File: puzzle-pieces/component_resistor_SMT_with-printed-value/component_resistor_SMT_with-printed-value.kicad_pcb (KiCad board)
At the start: 2 copper layers, 40 x 40 mm, 11 parts, among them J1 Conn_01x02_Pin, J2 Conn_01x02_Pin

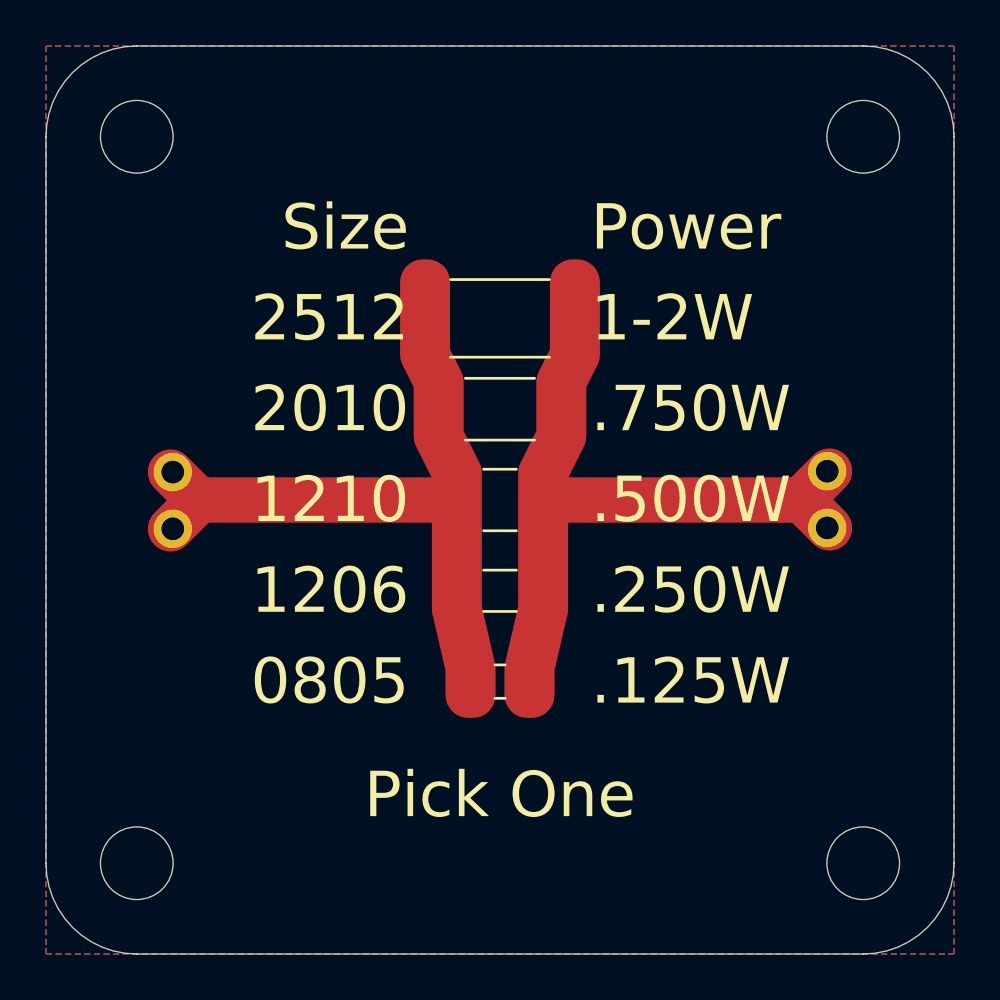
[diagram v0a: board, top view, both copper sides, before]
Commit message: Update resistor footprints and add THT 3W production files
Replaced mounting hole footprints with SMD resistor footprints in the SMT E-6 series panel and updated net assignments. Added new KiCad PCB, project, and production ZIP files for the THT 3W E-6 series resistors. Updated connector reference and position in the SMT panel.
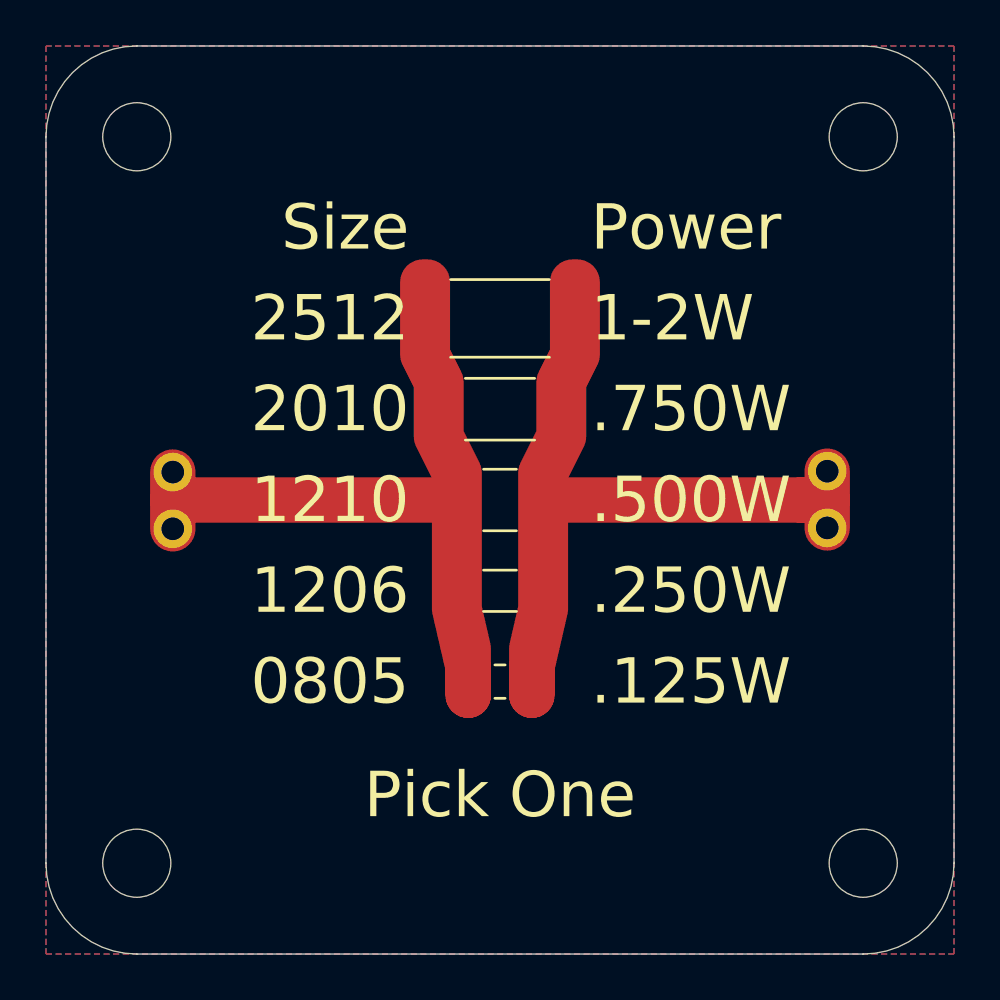
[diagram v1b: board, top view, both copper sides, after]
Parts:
- H1, H2, H3, H4: footprint MountingHole:MountingHole_3.2mm_M3 -> EASYEDA2KICAD:MountingHole_3.0mm_M3_tight
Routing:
- net Net-(J2-Pin_1): track 14.8 -> 16.0 mm
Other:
- board text added: "10 Ω"
- board text removed: "470 Ω"

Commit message: Update resistor value and PCB artwork to 10kΩ
Changed the silkscreen text from '10Ω' to '10kΩ' and updated associated PCB artwork and mask color definitions. Modified polygon and text elements in the KiCad PCB file and replaced the TOP and BOTTOM PNG images to reflect the new value and design.
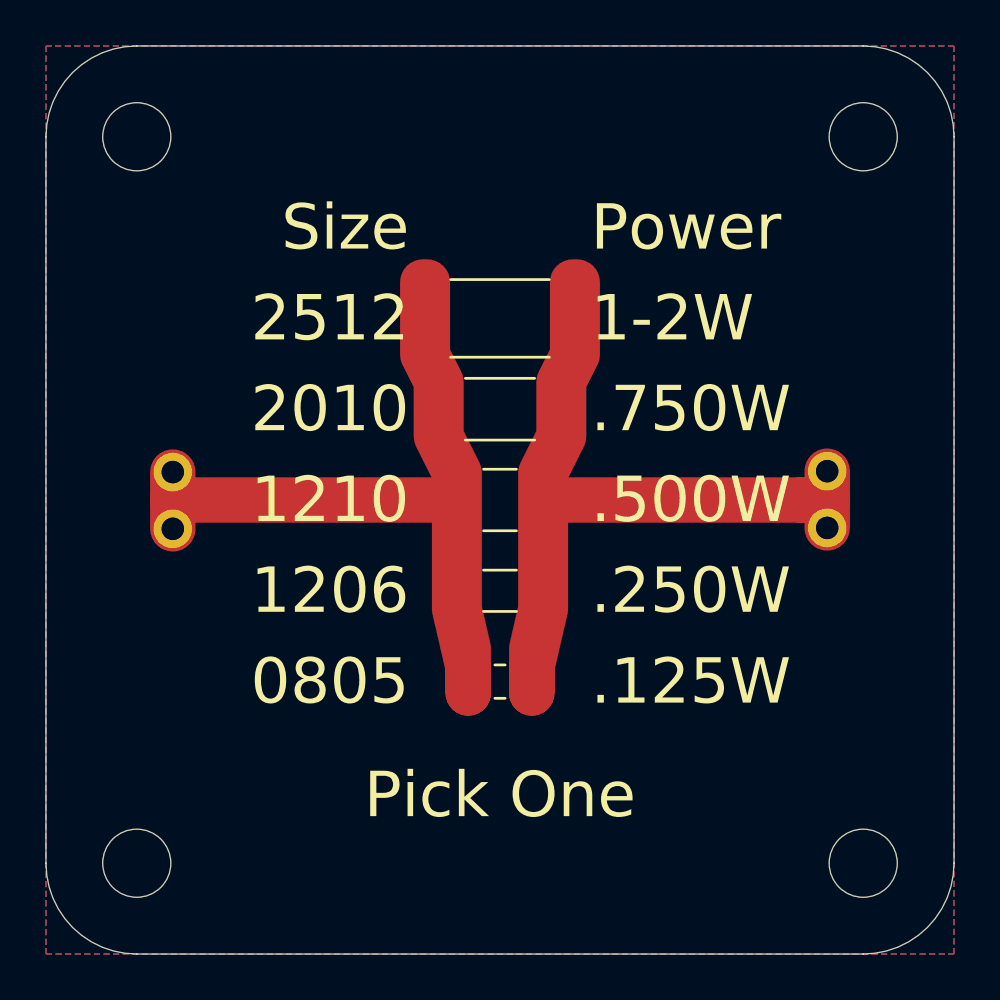
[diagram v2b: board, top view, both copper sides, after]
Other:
- board text added: "10 kΩ"
- board text removed: "10 Ω"
